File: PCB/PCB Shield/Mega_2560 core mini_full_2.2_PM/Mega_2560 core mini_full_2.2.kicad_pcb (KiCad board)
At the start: 2 copper layers, 89.5 x 59.7 mm, 146 parts, among them P1 2560-core, P10 RX1TX1, P11 Trim, P12 Stick_left, P13 Stick_right, P14 Switch, P15 Micro_sd, P16 LCD, P17 BATT, P18 Ecolage, P19 Module_Tx, P2 LCD_I2C, P20 TTL/RS232, P21 Sw_power, P22 JQ6500_28P, P23 Rot_1, P24 Rot_2, P25 Keys, P26 LCD_Alim, P28 5v/3,3v manches, P3 FTDI, P30 MiniDCDC3A, P31 Pot2, P32 Pot1, P4 Pot3, P5 Vibreur, P6 SPI, P7 SPIX, P8 Audio, P9 DUMMY, Q1 IRLML5203, Q2 MMBT2222ALT1, Q3 MMBT2222ALT1, Q4 SI2319DS, U1 74LVC1G3157GV, U2 74LVC1G3157GV, U3 74LVC1G3157GV, U4 PM5033, U5 LD1117S33TR, U6 MCP6004, U7 FM24W256, U8 DS3231SN

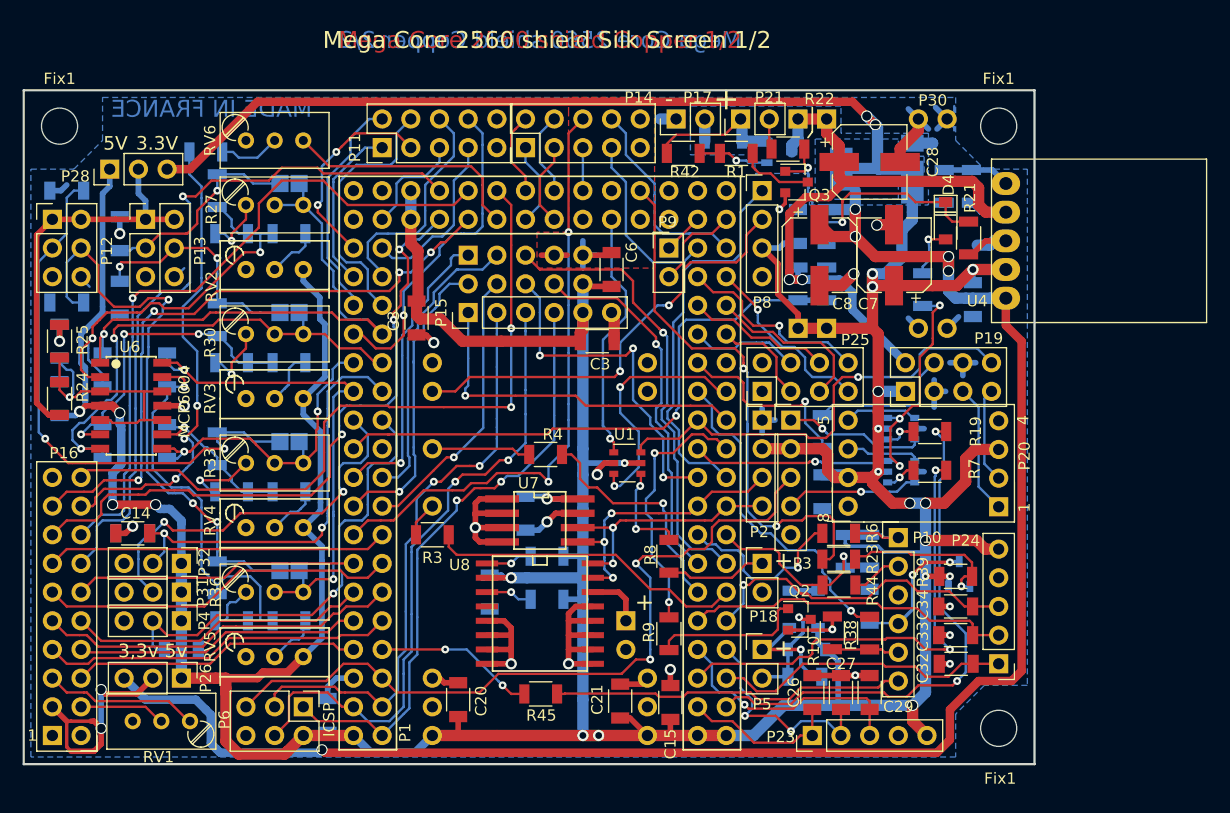
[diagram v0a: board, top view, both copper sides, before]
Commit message: Add SCC feature for SBUS servo programmation
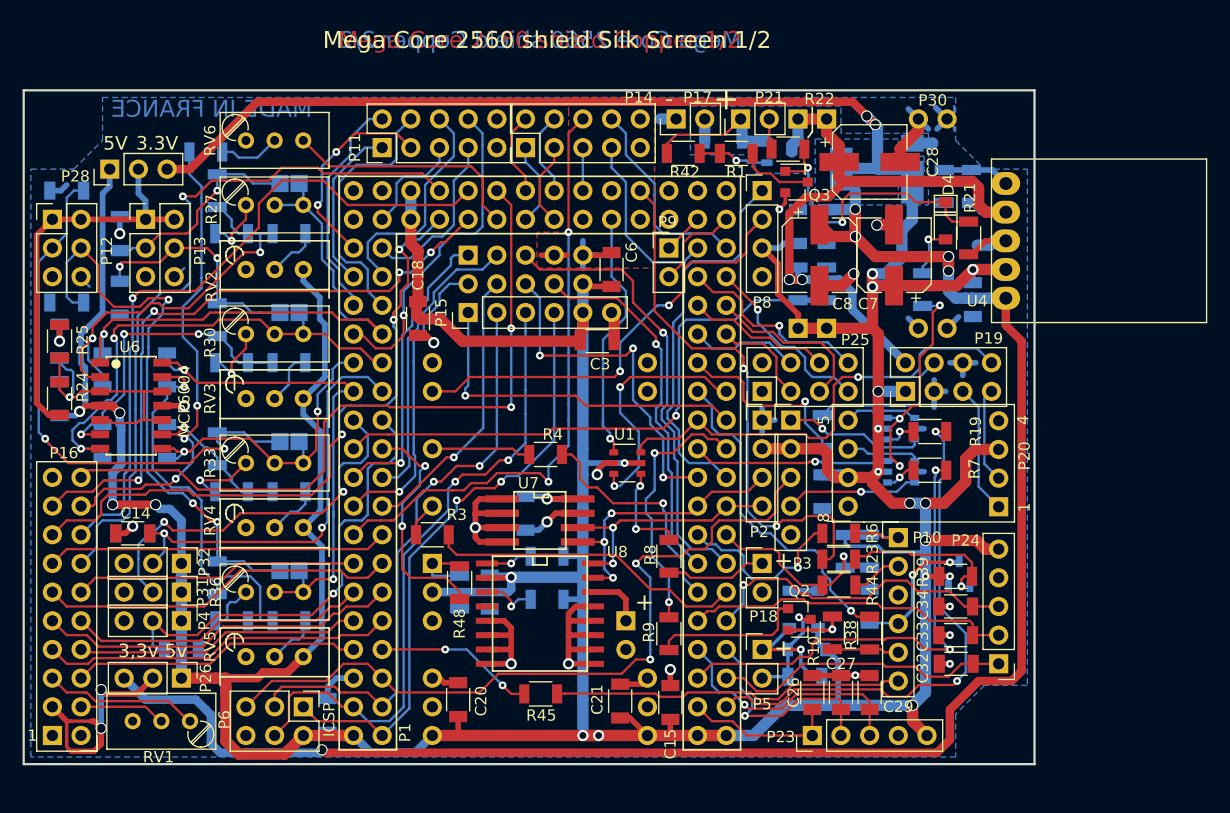
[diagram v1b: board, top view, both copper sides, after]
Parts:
- removed the C3 at (175.0, 82.0)
- removed the C3 at (191.0, 84.1)
- removed Fix1 (x3): MountingHole_3.2mm_M3, Mega_2560 core mini_full_2:MountingHole_3.2mm_M3
- removed REF**: WEEE-Logo_4.2x6mm_SilkScreen, Symbol:WEEE-Logo_4.2x6mm_SilkScreen
- removed REF**: OSHW-Logo2_7.3x6mm_SilkScreen, Symbol:OSHW-Logo2_7.3x6mm_SilkScreen
- added C18: 100nF, Mylib_v2.2:C_1206, F.Cu at (175.1, 82.1)
- added C3: 100nF, Mylib_v2.2:C_1206, F.Cu at (191.0, 84.1)
- added P27: SCC, Mylib_v2.2:Pin_Header_Straight_1x03_Pitch2.54mm, B.Cu at (176.4, 103.8)
- added R47: 100K, Mylib_v2.2:R_1206, B.Cu at (178.8, 106.3)
- added R48: 1K, Mylib_v2.2:R_1206, F.Cu at (178.8, 105.5)
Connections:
- P1 pad J2: (no net) -> SCC
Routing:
- net SCC: track 0.00 -> 21.0 mm, vias 0 -> 2
- net VCC: track 434.4 -> 442.6 mm
- net Net-(P27-Pad1): track 0.00 -> 6.00 mm
- net Net-(R15-Pad1): track 4.13 -> 4.95 mm
- net Rot_1push: track 14.0 -> 13.5 mm
- net Rot_1B: track 19.4 -> 19.3 mm, vias 2 -> 1
